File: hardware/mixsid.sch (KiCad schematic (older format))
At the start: 69 parts, among them P1 INPUT, P2 CONTROL, P4 SOCKET LEFT, P5 OUTPUT, P6 SOCKET RIGHT, Q1 BC547, Q2 BC547, U1 GAL16V8, U2 SID2, U3 7812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

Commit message: Hardware: Fixed connection and orientation of volume pots
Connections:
- net GND: now also RV3.1, RV4.1; no longer RV3.3, RV4.3
- net at C19.2: now also RV3.3; no longer RV3.1
- net at C22.2: now also RV4.3; no longer RV4.1
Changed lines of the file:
@@
 F 3 "" H 4100 4300 60  0000 C CNN
 	1    4100 4300
-	0    1    1    0
+	0    1    -1   0
 $EndComp
 $Comp
@@
 F 3 "" H 7050 4350 60  0000 C CNN
 	1    7050 4350
-	0    1    1    0
+	0    1    -1   0
 $EndComp
 $Comp

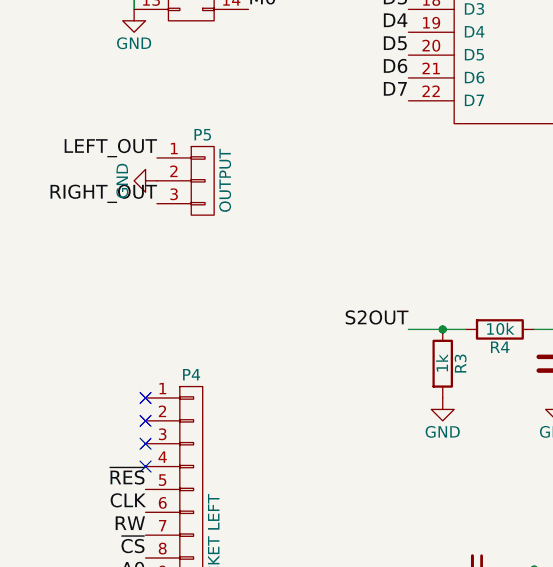
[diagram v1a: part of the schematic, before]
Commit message: Hardware: Added pin header to access raw audio out as well
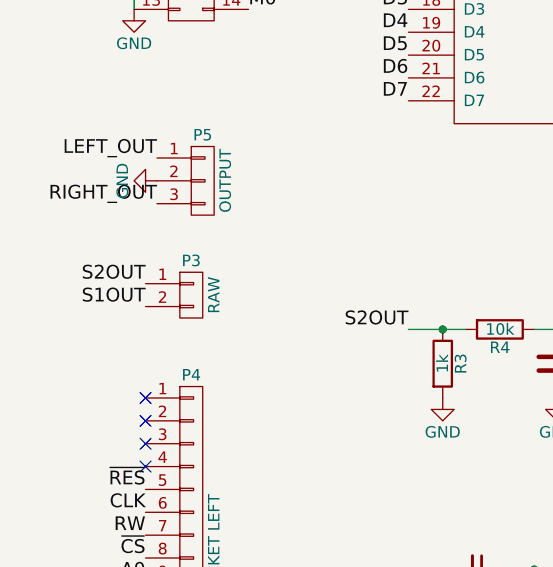
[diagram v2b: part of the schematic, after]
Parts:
- added P3: RAW, Pinheaders:Pin_Header_Straight_1x02, symbol CONN_01X02
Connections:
- net S1OUT: now also P3.2 (P2)
- net S2OUT: now also P3.1 (P1)
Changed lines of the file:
@@
 Text Label 1450 2150 0    60   ~ 0
 ~RW2
+$Comp
+L CONN_01X02 P3
+U 1 1 5732EF33
+P 1200 3600
+F 0 "P3" H 1200 3750 50  0000 C CNN
+F 1 "RAW" V 1300 3600 50  0000 C CNN
+F 2 "Pinheaders:Pin_Header_Straight_1x02" H 1200 3600 60  0001 C CNN
+F 3 "" H 1200 3600 60  0000 C CNN
+	1    1200 3600
+	1    0    0    -1
+$EndComp
+Text Label 1000 3550 2    60   ~ 0
+S2OUT
+Text Label 1000 3650 2    60   ~ 0
+S1OUT
 $EndSCHEMATC

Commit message: Hardware: Improved routing and silkscreen
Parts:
- U1: footprint Housings_DIP:DIP-20_W7.62mm -> Pinheaders:DIP-20_W7.62mm
- U2, U5: footprint Housings_DIP:DIP-28_W15.24mm -> Pinheaders:DIP-28_W15.24mm
- U6, U7: footprint Housings_DIP:DIP-16_W7.62mm -> Pinheaders:DIP-16_W7.62mm
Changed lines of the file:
@@
 F 0 "U5" H 5400 2950 60  0000 C CNN
 F 1 "SID1" H 6000 800 60  0000 C CNN
-F 2 "Housings_DIP:DIP-28_W15.24mm" H 5950 1950 60  0001 C CNN
+F 2 "Pinheaders:DIP-28_W15.24mm" H 5950 1950 60  0001 C CNN
 F 3 "" H 5950 1950 60  0000 C CNN
 	1    5750 1900
@@
 F 0 "U2" H 2400 2900 60  0000 C CNN
 F 1 "SID2" H 3000 750 60  0000 C CNN
-F 2 "Housings_DIP:DIP-28_W15.24mm" H 2950 1900 60  0001 C CNN
+F 2 "Pinheaders:DIP-28_W15.24mm" H 2950 1900 60  0001 C CNN
 F 3 "" H 2950 1900 60  0000 C CNN
 	1    2750 1850
@@
 F 0 "U6" H 10050 5650 60  0000 C CNN
 F 1 "4052" H 10050 5450 60  0000 C CNN
-F 2 "Housings_DIP:DIP-16_W7.62mm" H 9950 5650 60  0001 C CNN
+F 2 "Pinheaders:DIP-16_W7.62mm" H 9950 5650 60  0001 C CNN
 F 3 "" H 9950 5650 60  0000 C CNN
 	1    9950 5650
@@
 F 0 "U1" H 7450 6400 60  0000 C CNN
 F 1 "GAL16V8" H 7450 5300 60  0000 C CNN
-F 2 "Housings_DIP:DIP-20_W7.62mm" H 7500 5600 60  0001 C CNN
+F 2 "Pinheaders:DIP-20_W7.62mm" H 7500 5600 60  0001 C CNN
 F 3 "" H 7500 5600 60  0000 C CNN
 	1    7450 5850
@@
 F 0 "U7" H 9450 3450 60  0000 C CNN
 F 1 "4053" H 9450 3250 60  0000 C CNN
-F 2 "Housings_DIP:DIP-16_W7.62mm" H 9350 3450 60  0001 C CNN
+F 2 "Pinheaders:DIP-16_W7.62mm" H 9350 3450 60  0001 C CNN
 F 3 "" H 9350 3450 60  0000 C CNN
 	1    9350 3450

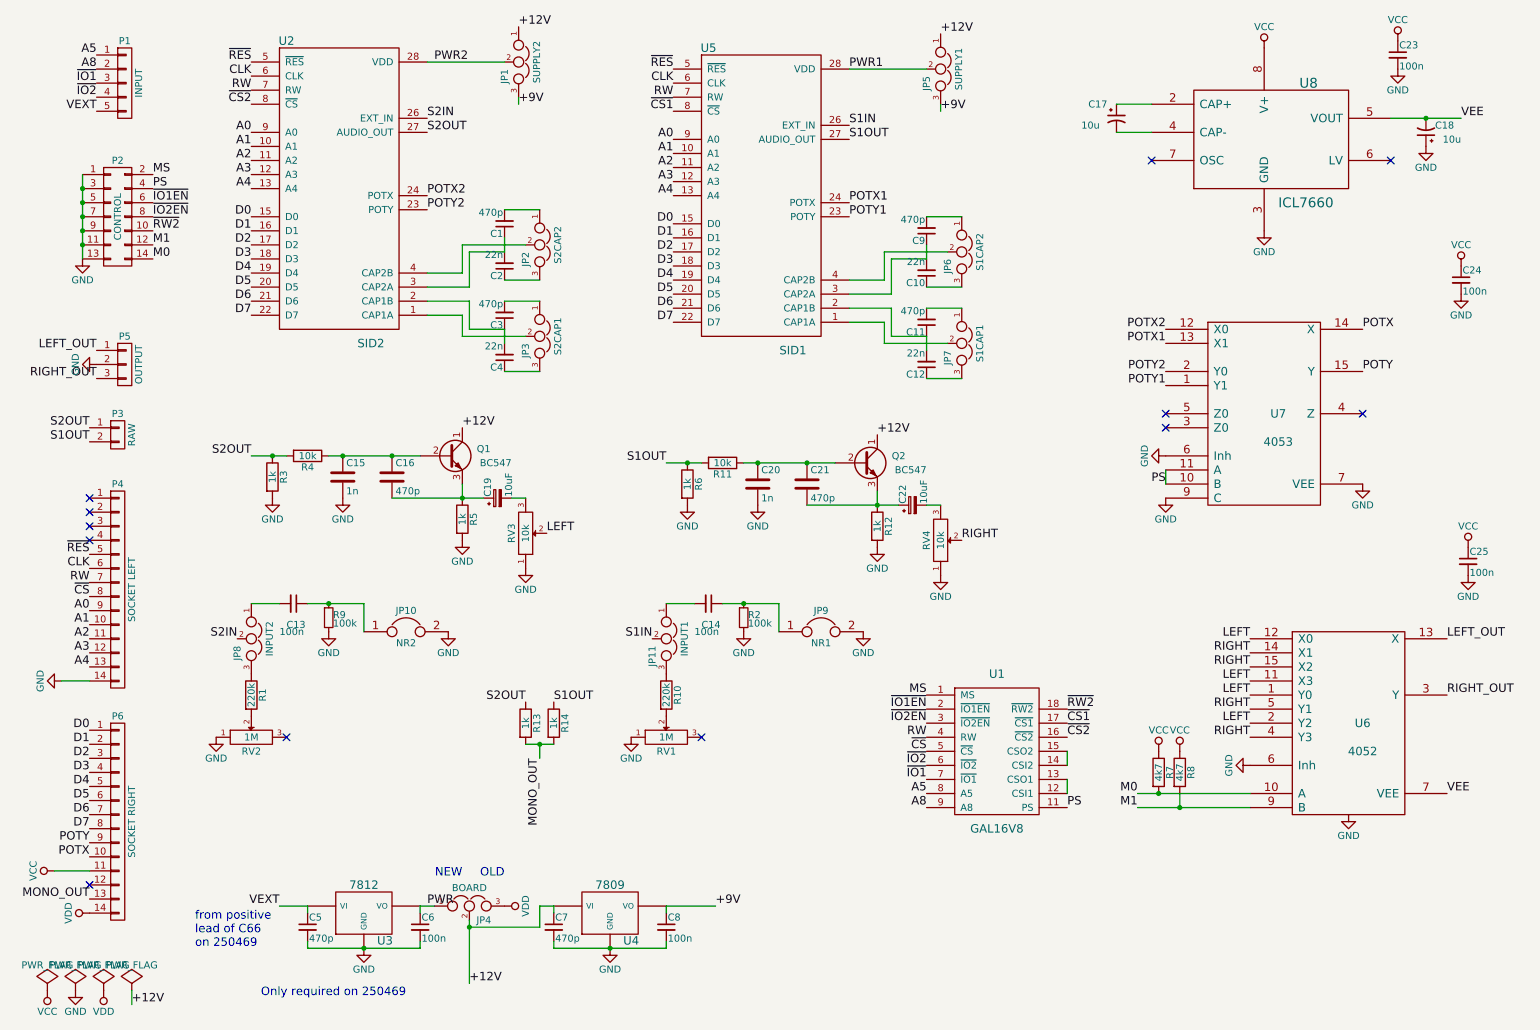
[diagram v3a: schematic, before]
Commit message: Hardware: Added -5V test point, improved silkscreen
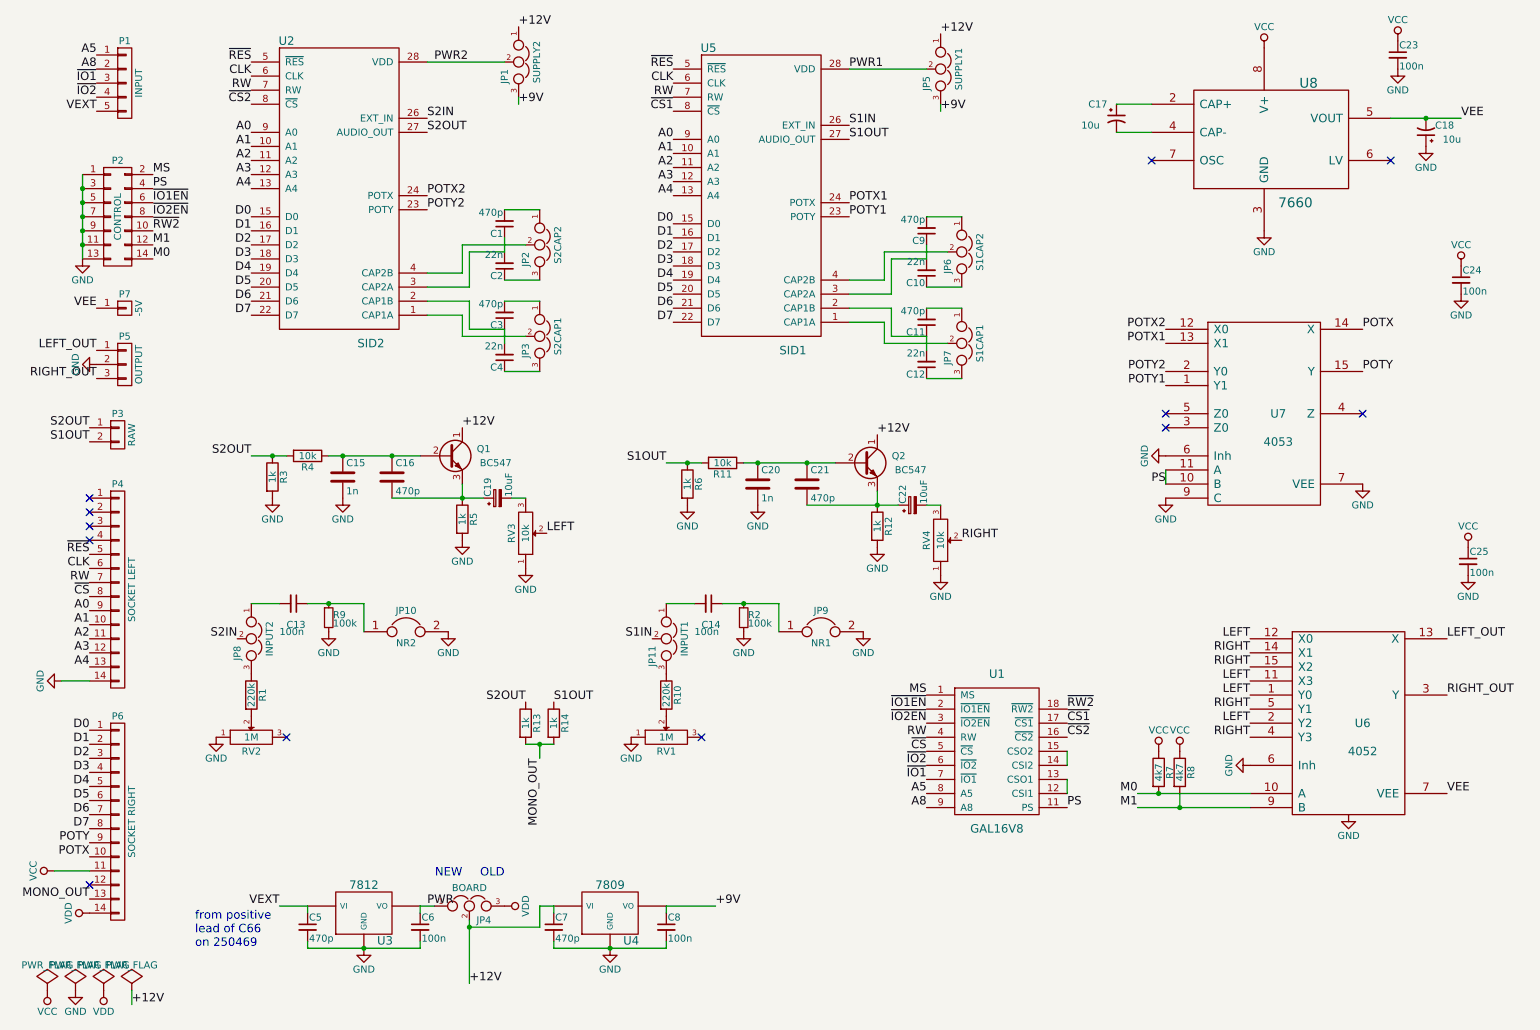
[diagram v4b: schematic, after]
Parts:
- added P7: -5V, Measurement_Points:Measurement_Point_Round-TH_Small, symbol CONN_01X01
- C1, C10, C11, C12, C13, C14, C15, C16, C2, C20, C21, C23, C24, C25, C3, C4, C5, C6, C7, C8, C9: footprint Capacitors_ThroughHole:C_Disc_D3_P2.5 -> Pinheaders:C_Disc_D3_P2.5
- U8: value ICL7660 -> 7660
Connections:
- net VEE: now also P7.1 (P1)
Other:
- note removed: "Only required on 250469"
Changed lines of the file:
@@
 Title "MixSID - C64 stereo SID addon board"
 Date "2016-03-09"
-Rev "1"
+Rev "3"
 Comp "Henning Bekel"
 Comment1 ""
@@
 F 0 "C2" H 3960 2470 50  0000 L CNN
 F 1 "22n" H 3960 2320 50  0000 L CNN
-F 2 "Capacitors_ThroughHole:C_Disc_D3_P2.5" H 3950 2400 60  0001 C CNN
+F 2 "Pinheaders:C_Disc_D3_P2.5" H 3950 2400 60  0001 C CNN
 F 3 "" H 3950 2400 60  0000 C CNN
 	1    3950 2400
@@
 F 0 "C1" H 3960 2170 50  0000 L CNN
 F 1 "470p" H 3960 2020 50  0000 L CNN
-F 2 "Capacitors_ThroughHole:C_Disc_D3_P2.5" H 3950 2100 60  0001 C CNN
+F 2 "Pinheaders:C_Disc_D3_P2.5" H 3950 2100 60  0001 C CNN
 F 3 "" H 3950 2100 60  0000 C CNN
 	1    3950 2100
@@
 F 0 "C4" H 3960 3120 50  0000 L CNN
 F 1 "22n" H 3960 2970 50  0000 L CNN
-F 2 "Capacitors_ThroughHole:C_Disc_D3_P2.5" H 3950 3050 60  0001 C CNN
+F 2 "Pinheaders:C_Disc_D3_P2.5" H 3950 3050 60  0001 C CNN
 F 3 "" H 3950 3050 60  0000 C CNN
 	1    3950 3050
@@
 F 0 "C3" H 3960 2820 50  0000 L CNN
 F 1 "470p" H 3960 2670 50  0000 L CNN
-F 2 "Capacitors_ThroughHole:C_Disc_D3_P2.5" H 3950 2750 60  0001 C CNN
+F 2 "Pinheaders:C_Disc_D3_P2.5" H 3950 2750 60  0001 C CNN
 F 3 "" H 3950 2750 60  0000 C CNN
 	1    3950 2750
@@
 F 0 "C10" H 6960 2520 50  0000 L CNN
 F 1 "22n" H 6960 2370 50  0000 L CNN
-F 2 "Capacitors_ThroughHole:C_Disc_D3_P2.5" H 6950 2450 60  0001 C CNN
+F 2 "Pinheaders:C_Disc_D3_P2.5" H 6950 2450 60  0001 C CNN
 F 3 "" H 6950 2450 60  0000 C CNN
 	1    6950 2450
@@
 F 0 "C9" H 6960 2220 50  0000 L CNN
 F 1 "470p" H 6960 2070 50  0000 L CNN
-F 2 "Capacitors_ThroughHole:C_Disc_D3_P2.5" H 6950 2150 60  0001 C CNN
+F 2 "Pinheaders:C_Disc_D3_P2.5" H 6950 2150 60  0001 C CNN
 F 3 "" H 6950 2150 60  0000 C CNN
 	1    6950 2150
@@
 F 0 "C12" H 6960 3170 50  0000 L CNN
 F 1 "22n" H 6960 3020 50  0000 L CNN
-F 2 "Capacitors_ThroughHole:C_Disc_D3_P2.5" H 6950 3100 60  0001 C CNN
+F 2 "Pinheaders:C_Disc_D3_P2.5" H 6950 3100 60  0001 C CNN
 F 3 "" H 6950 3100 60  0000 C CNN
 	1    6950 3100
@@
 F 0 "C11" H 6960 2870 50  0000 L CNN
 F 1 "470p" H 6960 2720 50  0000 L CNN
-F 2 "Capacitors_ThroughHole:C_Disc_D3_P2.5" H 6950 2800 60  0001 C CNN
+F 2 "Pinheaders:C_Disc_D3_P2.5" H 6950 2800 60  0001 C CNN
 F 3 "" H 6950 2800 60  0000 C CNN
 	1    6950 2800
@@
 F 0 "C5" H 2560 7170 50  0000 L CNN
 F 1 "470p" H 2560 7020 50  0000 L CNN
-F 2 "Capacitors_ThroughHole:C_Disc_D3_P2.5" H 2550 7100 60  0001 C CNN
+F 2 "Pinheaders:C_Disc_D3_P2.5" H 2550 7100 60  0001 C CNN
 F 3 "" H 2550 7100 60  0000 C CNN
 	1    2550 7100
@@
 F 0 "C6" H 3360 7170 50  0000 L CNN
 F 1 "100n" H 3360 7020 50  0000 L CNN
-F 2 "Capacitors_ThroughHole:C_Disc_D3_P2.5" H 3350 7100 60  0001 C CNN
+F 2 "Pinheaders:C_Disc_D3_P2.5" H 3350 7100 60  0001 C CNN
 F 3 "" H 3350 7100 60  0000 C CNN
 	1    3350 7100
@@
 F 0 "C7" H 4310 7170 50  0000 L CNN
 F 1 "470p" H 4310 7020 50  0000 L CNN
-F 2 "Capacitors_ThroughHole:C_Disc_D3_P2.5" H 4300 7100 60  0001 C CNN
+F 2 "Pinheaders:C_Disc_D3_P2.5" H 4300 7100 60  0001 C CNN
 F 3 "" H 4300 7100 60  0000 C CNN
 	1    4300 7100
@@
 F 0 "C8" H 5110 7170 50  0000 L CNN
 F 1 "100n" H 5110 7020 50  0000 L CNN
-F 2 "Capacitors_ThroughHole:C_Disc_D3_P2.5" H 5100 7100 60  0001 C CNN
+F 2 "Pinheaders:C_Disc_D3_P2.5" H 5100 7100 60  0001 C CNN
 F 3 "" H 5100 7100 60  0000 C CNN
 	1    5100 7100
@@
 F 0 "C14" V 5550 4750 50  0000 L CNN
 F 1 "100n" V 5600 4700 50  0000 L CNN
-F 2 "Capacitors_ThroughHole:C_Disc_D3_P2.5" H 5400 4800 60  0001 C CNN
+F 2 "Pinheaders:C_Disc_D3_P2.5" H 5400 4800 60  0001 C CNN
 F 3 "" H 5400 4800 60  0000 C CNN
 	1    5400 4800
@@
 Text Label 1450 2250 0    60   ~ 0
 M1
-Text Notes 3250 7600 2    60   ~ 0
-Only required on 250469
 Text Notes 1750 7250 0    60   ~ 0
 from positive \nlead of C66\non 250469
@@
 P 9400 1500
 F 0 "U8" H 9600 1900 70  0000 L CNN
-F 1 "ICL7660" H 9450 1050 70  0000 L CNN
+F 1 "7660" H 9450 1050 70  0000 L CNN
 F 2 "Pinheaders:DIP-8_W7.62mm" H 9400 1500 60  0001 C CNN
 F 3 "" H 9400 1500 60  0000 C CNN
@@
 F 0 "C13" V 2600 4750 50  0000 L CNN
 F 1 "100n" V 2650 4700 50  0000 L CNN
-F 2 "Capacitors_ThroughHole:C_Disc_D3_P2.5" H 2450 4800 60  0001 C CNN
+F 2 "Pinheaders:C_Disc_D3_P2.5" H 2450 4800 60  0001 C CNN
 F 3 "" H 2450 4800 60  0000 C CNN
 	1    2450 4800
@@
 F 0 "C15" H 2825 4000 50  0000 L CNN
 F 1 "1n" H 2825 3800 50  0000 L CNN
-F 2 "Capacitors_ThroughHole:C_Disc_D3_P2.5" H 2838 3750 30  0001 C CNN
+F 2 "Pinheaders:C_Disc_D3_P2.5" H 2838 3750 30  0001 C CNN
 F 3 "" H 2800 3900 60  0000 C CNN
 	1    2800 3900
@@
 F 0 "C16" H 3175 4000 50  0000 L CNN
 F 1 "470p" H 3175 3800 50  0000 L CNN
-F 2 "Capacitors_ThroughHole:C_Disc_D3_P2.5" H 3188 3750 30  0001 C CNN
+F 2 "Pinheaders:C_Disc_D3_P2.5" H 3188 3750 30  0001 C CNN
 F 3 "" H 3150 3900 60  0000 C CNN
 	1    3150 3900
@@
 F 0 "C20" H 5775 4050 50  0000 L CNN
 F 1 "1n" H 5775 3850 50  0000 L CNN
-F 2 "Capacitors_ThroughHole:C_Disc_D3_P2.5" H 5788 3800 30  0001 C CNN
+F 2 "Pinheaders:C_Disc_D3_P2.5" H 5788 3800 30  0001 C CNN
 F 3 "" H 5750 3950 60  0000 C CNN
 	1    5750 3950
@@
 F 0 "C21" H 6125 4050 50  0000 L CNN
 F 1 "470p" H 6125 3850 50  0000 L CNN
-F 2 "Capacitors_ThroughHole:C_Disc_D3_P2.5" H 6138 3800 30  0001 C CNN
+F 2 "Pinheaders:C_Disc_D3_P2.5" H 6138 3800 30  0001 C CNN
 F 3 "" H 6100 3950 60  0000 C CNN
 	1    6100 3950
@@
 F 0 "C25" H 10810 4570 50  0000 L CNN
 F 1 "100n" H 10810 4420 50  0000 L CNN
-F 2 "Capacitors_ThroughHole:C_Disc_D3_P2.5" H 10800 4500 60  0001 C CNN
+F 2 "Pinheaders:C_Disc_D3_P2.5" H 10800 4500 60  0001 C CNN
 F 3 "" H 10800 4500 60  0000 C CNN
 	1    10800 4500
@@
 F 0 "C24" H 10760 2570 50  0000 L CNN
 F 1 "100n" H 10760 2420 50  0000 L CNN
-F 2 "Capacitors_ThroughHole:C_Disc_D3_P2.5" H 10750 2500 60  0001 C CNN
+F 2 "Pinheaders:C_Disc_D3_P2.5" H 10750 2500 60  0001 C CNN
 F 3 "" H 10750 2500 60  0000 C CNN
 	1    10750 2500
@@
 F 0 "C23" H 10310 970 50  0000 L CNN
 F 1 "100n" H 10310 820 50  0000 L CNN
-F 2 "Capacitors_ThroughHole:C_Disc_D3_P2.5" H 10300 900 60  0001 C CNN
+F 2 "Pinheaders:C_Disc_D3_P2.5" H 10300 900 60  0001 C CNN
 F 3 "" H 10300 900 60  0000 C CNN
 	1    10300 900
@@
 Text Label 1000 3650 2    60   ~ 0
 S1OUT
+$Comp
+L CONN_01X01 P7
+U 1 1 57334D37
+P 1250 2700
+F 0 "P7" H 1250 2800 50  0000 C CNN
+F 1 "-5V" V 1350 2700 50  0000 C CNN
+F 2 "Measurement_Points:Measurement_Point_Round-TH_Small" H 1250 2700 60  0001 C CNN
+F 3 "" H 1250 2700 60  0000 C CNN
+	1    1250 2700
+	1    0    0    -1
+$EndComp
+Text Label 1050 2700 2    60   ~ 0
+VEE
 $EndSCHEMATC
